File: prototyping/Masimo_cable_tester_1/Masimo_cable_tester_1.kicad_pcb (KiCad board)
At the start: 2 copper layers, 70 x 80 mm, 28 parts, among them J1 Touchscreen HMI, J10 MCU Board Power, J16 Debug Connections, J17 Banana Jack, J2 Curiosity Nano AVR128DB48, J3 Conn_01x28_Socket, J4 Barrel Jack 9V, J5 MicroSD PinHeader, J6 SFML-110-02-L-D-A, J7 HMI Power Toggle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

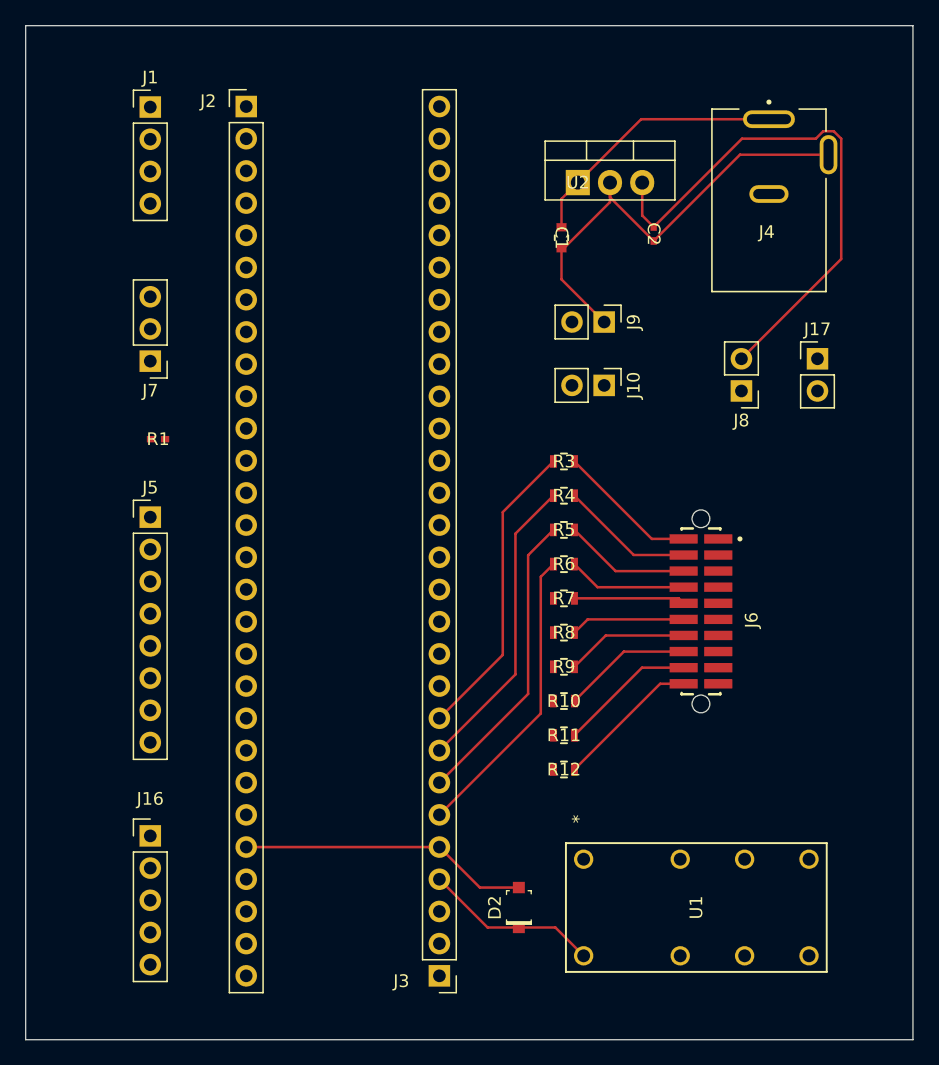
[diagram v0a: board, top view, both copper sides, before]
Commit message: Prototype Schematic and PCB Update
Updated the prototype schematic and PCB. Put all analog if tags on 1 side for easier PCB tracing. By doing this I also changed the location of the Rsig, CD, and CS locations on the MC.
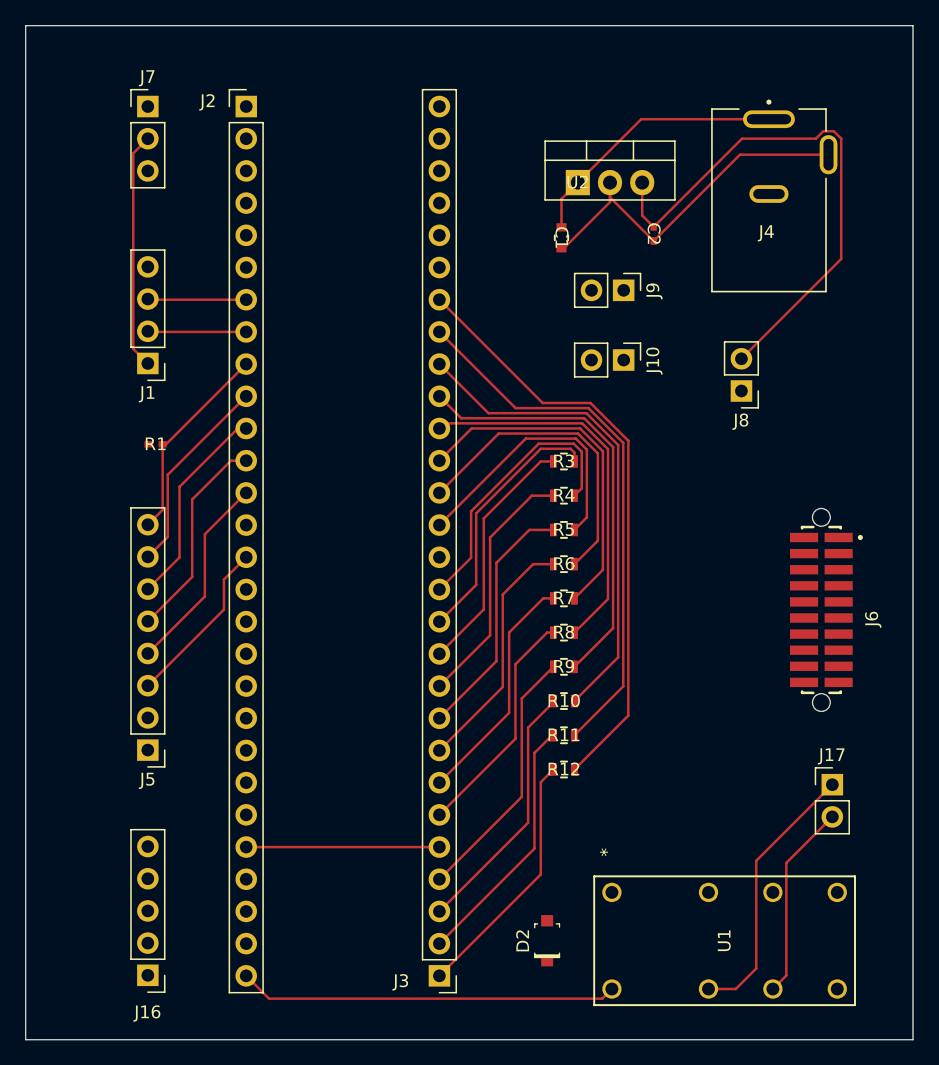
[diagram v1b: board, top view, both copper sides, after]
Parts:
- moved J17 33.6 mm to (144.0, 111.5)
- moved J1 20.2 mm to (90.0, 78.3), turned to 180 degrees
- moved J7 20.1 mm to (90.0, 58.0), turned to 0 degrees
- moved J5 18.4 mm to (90.0, 108.8), turned to 180 degrees
- moved J16 11.0 mm to (90.0, 126.5), turned to 180 degrees
- moved J6 9.50 mm to (143.1, 97.7)
- moved D2 3.44 mm to (121.5, 123.8)
- moved U1 3.44 mm to (126.6, 127.6)
- moved J9 2.94 mm to (127.5, 72.5)
- moved J10 2.52 mm to (127.5, 78.0)
- moved R1 0.45 mm to (90.6, 84.6)
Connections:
- J17 pad 2: BJ1 -> BJ2
- J2 pad 10: unconnected-(J2-Pin_10-Pad10) -> CS
- J2 pad 18: CTRL 10 -> unconnected-(J2-Pin_18-Pad18)
- J2 pad 19: CTRL 9 -> unconnected-(J2-Pin_19-Pad19)
- J2 pad 20: CTRL 8 -> unconnected-(J2-Pin_20-Pad20)
- J2 pad 21: CTRL 7 -> unconnected-(J2-Pin_21-Pad21)
- J2 pad 22: CTRL 6 -> unconnected-(J2-Pin_22-Pad22)
- J2 pad 23: CTRL 5 -> unconnected-(J2-Pin_23-Pad23)
- J2 pad 28: unconnected-(J2-Pin_28-Pad28) -> RSig
- J2 pad 9: unconnected-(J2-Pin_9-Pad9) -> CD
- J3 pad 1: unconnected-(J3-Pin_1-Pad1) -> CTRL 10
- J3 pad 10: ADC 10 -> CTRL 2
- J3 pad 11: ADC 9 -> CTRL 1
- J3 pad 12: CS -> ADC 1
- J3 pad 13: CD -> ADC 2
- J3 pad 15: ADC 8 -> ADC 3
- J3 pad 16: ADC 7 -> ADC 4
- J3 pad 17: ADC 6 -> ADC 5
- J3 pad 18: ADC 5 -> ADC 6
- J3 pad 19: ADC 4 -> ADC 7
- J3 pad 2: unconnected-(J3-Pin_2-Pad2) -> CTRL 9
- J3 pad 20: ADC 3 -> ADC 8
- J3 pad 21: ADC 2 -> ADC 9
- J3 pad 22: ADC 1 -> ADC 10
- J3 pad 3: unconnected-(J3-Pin_3-Pad3) -> CTRL 8
- J3 pad 4: RSig -> CTRL 7
- J3 pad 6: CTRL 4 -> CTRL 6
- J3 pad 7: CTRL 3 -> CTRL 5
- J3 pad 8: CTRL 2 -> CTRL 4
- J3 pad 9: CTRL 1 -> CTRL 3
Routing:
- net ADC 10: track 11.4 -> 47.2 mm
- net ADC 9: track 10.8 -> 42.8 mm
- net ADC 8: track 10.2 -> 38.4 mm
- net ADC 7: track 9.64 -> 34.0 mm
- net BJ1: track 0.00 -> 21.4 mm
- net ADC 6: track 9.05 -> 29.9 mm
- net CTRL 7: track 0.00 -> 20.5 mm
- net CTRL 8: track 0.00 -> 20.3 mm
- net CTRL 9: track 0.00 -> 20.2 mm
- net CTRL 10: track 0.00 -> 20.0 mm
- net CTRL 5: track 0.00 -> 18.7 mm
- net Net-(J1-Pin_1): track 0.00 -> 18.7 mm
- net ADC 5: track 8.78 -> 27.2 mm
- net CTRL 6: track 0.00 -> 18.4 mm
- net DO: track 0.00 -> 16.6 mm
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
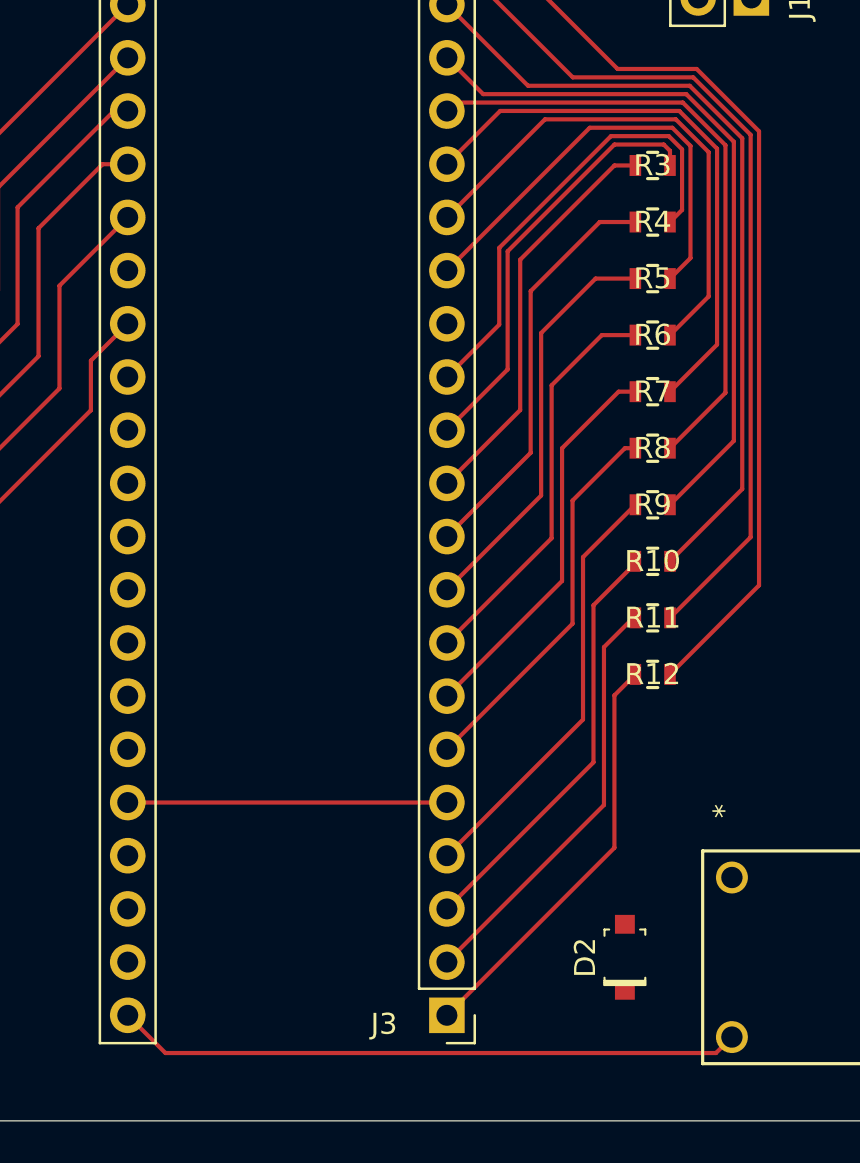
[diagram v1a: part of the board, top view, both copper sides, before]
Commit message: Prototype PCB Changes
A few routing changes to the Prototype PCB.
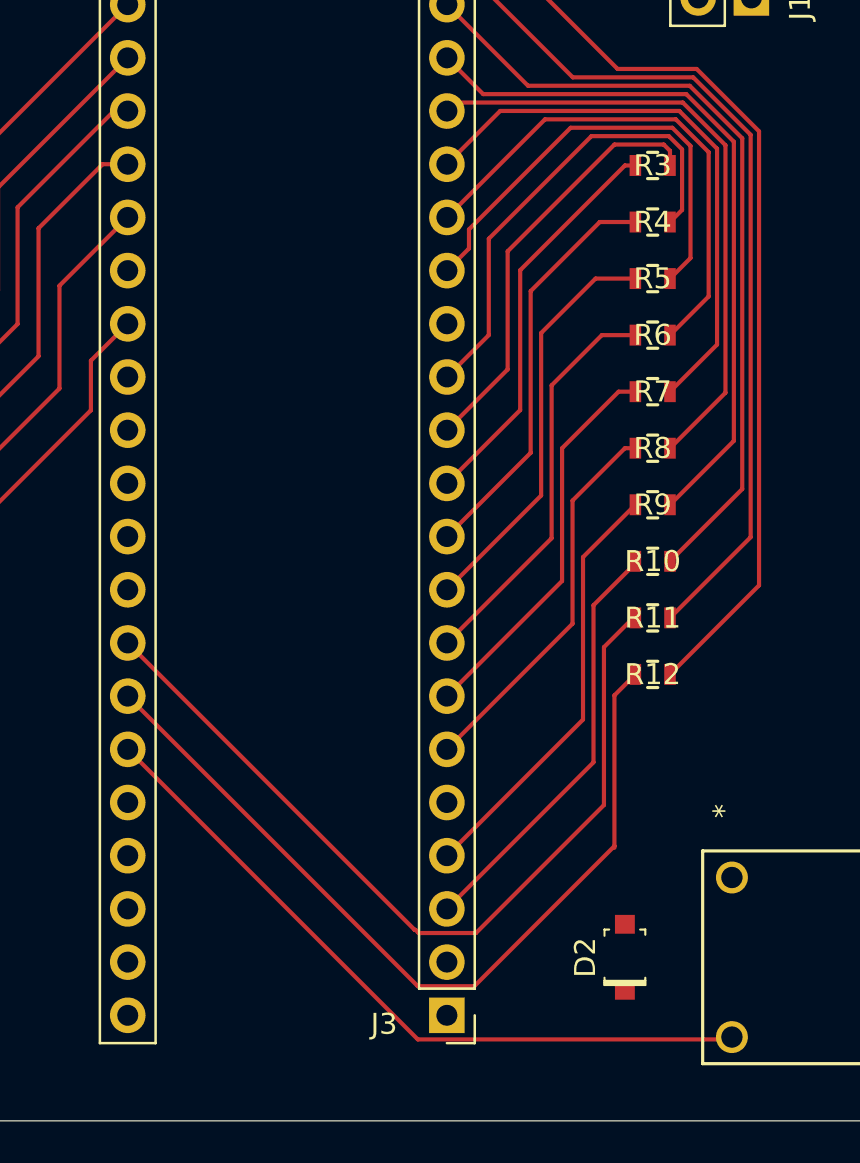
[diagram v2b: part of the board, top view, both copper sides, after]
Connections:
- J2 pad 21: unconnected-(J2-Pin_21-Pad21) -> CTRL 9
- J2 pad 22: unconnected-(J2-Pin_22-Pad22) -> CTRL 10
- J2 pad 23: unconnected-(J2-Pin_23-Pad23) -> RSig
- J2 pad 28: RSig -> unconnected-(J2-Pin_28-Pad28)
- J3 pad 1: CTRL 10 -> unconnected-(J3-Pin_1-Pad1)
- J3 pad 2: CTRL 9 -> unconnected-(J3-Pin_2-Pad2)
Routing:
- net CTRL 10: track 20.0 -> 40.4 mm
- net CTRL 9: track 20.2 -> 40.6 mm
- net GND: track 58.1 -> 42.9 mm
- net RSig: track 29.9 -> 34.6 mm
- net ADC 2: track 22.1 -> 22.7 mm
- net ADC 3: track 21.6 -> 22.1 mm
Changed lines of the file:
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@@
 	(net 7 "Rx1")
 	(net 8 "unconnected-(J2-Pin_17-Pad17)")
-	(net 9 "unconnected-(J2-Pin_23-Pad23)")
-	(net 10 "unconnected-(J2-Pin_22-Pad22)")
+	(net 9 "unconnected-(J2-Pin_28-Pad28)")
+	(net 10 "unconnected-(J3-Pin_1-Pad1)")
 	(net 11 "CTRL 5")
 	(net 12 "unconnected-(J2-Pin_6-Pad6)")
@@
 	(net 49 "ADC 4")
 	(net 50 "Net-(J10-Pin_1)")
-	(net 51 "unconnected-(J2-Pin_21-Pad21)")
+	(net 51 "unconnected-(J3-Pin_2-Pad2)")
 	(net 52 "ADC 6")
 	(net 53 "VBUS 5V")
@@
 			)
 			(remove_unused_layers no)
-			(net 51 "unconnected-(J2-Pin_21-Pad21)")
+			(net 17 "CTRL 9")
 			(pinfunction "Pin_21")
 			(pintype "passive")
@@
 			)
 			(remove_unused_layers no)
-			(net 10 "unconnected-(J2-Pin_22-Pad22)")
+			(net 25 "CTRL 10")
 			(pinfunction "Pin_22")
 			(pintype "passive")
@@
 			)
 			(remove_unused_layers no)
-			(net 9 "unconnected-(J2-Pin_23-Pad23)")
+			(net 4 "RSig")
 			(pinfunction "Pin_23")
 			(pintype "passive")
@@
 			)
 			(remove_unused_layers no)
-			(net 4 "RSig")
+			(net 9 "unconnected-(J2-Pin_28-Pad28)")
 			(pinfunction "Pin_28")
 			(pintype "passive")
@@
 			)
 			(remove_unused_layers no)
-			(net 25 "CTRL 10")
+			(net 10 "unconnected-(J3-Pin_1-Pad1)")
 			(pinfunction "Pin_1")
 			(pintype "passive")
@@
 			)
 			(remove_unused_layers no)
-			(net 17 "CTRL 9")
+			(net 51 "unconnected-(J3-Pin_2-Pad2)")
 			(pinfunction "Pin_2")
 			(pintype "passive")
@@
 	)
 	(segment
-		(start 97.76 116.42)
-		(end 113 116.42)
-		(width 0.2)
-		(layer "F.Cu")
-		(net 1)
-	)
-	(segment
 		(start 126.46 65.1606)
 		(end 126.46 64)
@@
 	)
 	(segment
-		(start 125.848001 128.381999)
-		(end 126.61 127.62)
+		(start 111.611 127.731)
+		(end 126.499 127.731)
 		(width 0.2)
 		(layer "F.Cu")
@@
 	)
 	(segment
-		(start 99.561999 128.381999)
-		(end 125.848001 128.381999)
+		(start 126.499 127.731)
+		(end 126.61 127.62)
 		(width 0.2)
 		(layer "F.Cu")
@@
 	)
 	(segment
-		(start 97.76 126.58)
-		(end 99.561999 128.381999)
+		(start 97.76 113.88)
+		(end 111.611 127.731)
 		(width 0.2)
 		(layer "F.Cu")
@@
 	)
 	(segment
-		(start 121.898224 107.601776)
-		(end 122 107.601776)
+		(start 111.5 122.5)
+		(end 111.651 122.651)
 		(width 0.2)
 		(layer "F.Cu")
@@
 	)
 	(segment
-		(start 113 124.04)
+		(start 114.389 122.651)
 		(end 120.5 116.54)
 		(width 0.2)
@@
 	)
 	(segment
+		(start 111.46 122.5)
+		(end 111.5 122.5)
+		(width 0.2)
+		(layer "F.Cu")
+		(net 17)
+	)
+	(segment
+		(start 97.76 108.8)
+		(end 111.46 122.5)
+		(width 0.2)
+		(layer "F.Cu")
+		(net 17)
+	)
+	(segment
+		(start 121.898224 107.601776)
+		(end 122 107.601776)
+		(width 0.2)
+		(layer "F.Cu")
+		(net 17)
+	)
+	(segment
 		(start 120.5 109)
 		(end 121.898224 107.601776)
@@
 	)
 	(segment
+		(start 111.651 122.651)
+		(end 114.389 122.651)
+		(width 0.2)
+		(layer "F.Cu")
+		(net 17)
+	)
+	(segment
 		(start 120.5 116.54)
 		(end 120.5 109)
@@
 	)
 	(segment
-		(start 113 126.58)
-		(end 121 118.58)
+		(start 121 118.5)
+		(end 121 111.302)
 		(width 0.2)
 		(layer "F.Cu")
@@
 	)
 	(segment
-		(start 121 118.58)
-		(end 121 111.302)
+		(start 114.309 125.191)
+		(end 121 118.5)
 		(width 0.2)
 		(layer "F.Cu")
@@
 	)
 	(segment
+		(start 97.76 111.34)
+		(end 111.611 125.191)
+		(width 0.2)
+		(layer "F.Cu")
+		(net 25)
+	)
+	(segment
+		(start 121 118.58)
+		(end 121 118.5)
+		(width 0.2)
+		(layer "F.Cu")
+		(net 25)
+	)
+	(segment
+		(start 111.611 125.191)
+		(end 114.309 125.191)
+		(width 0.2)
+		(layer "F.Cu")
+		(net 25)
+	)
+	(segment
 		(start 119.5 112.46)
 		(end 119.5 104.701332)
@@
 	)
 	(segment
-		(start 113 91.02)
-		(end 119.822 84.198)
+		(start 124.6318 90.421844)
+		(end 124.6318 85.0647)
 		(width 0.2)
 		(layer "F.Cu")
@@
 	)
 	(segment
-		(start 123.7651 84.198)
-		(end 124.6318 85.0647)
+		(start 114.05388 89.05388)
+		(end 114.05388 89.96612)
 		(width 0.2)
 		(layer "F.Cu")
@@
 	)
 	(segment
-		(start 124.6318 90.421844)
-		(end 123.6532 91.400444)
+		(start 124.6318 85.0647)
+		(end 123.7651 84.198)
 		(width 0.2)
 		(layer "F.Cu")
@@
 	)
 	(segment
-		(start 119.822 84.198)
-		(end 123.7651 84.198)
+		(start 123.6532 91.400444)
+		(end 124.6318 90.421844)
 		(width 0.2)
 		(layer "F.Cu")
@@
 	)
 	(segment
-		(start 124.6318 85.0647)
-		(end 124.6318 90.421844)
+		(start 123.7651 84.198)
+		(end 118.90976 84.198)
 		(width 0.2)
 		(layer "F.Cu")
@@
 	)
 	(segment
-		(start 115.5 89.9329)
-		(end 120.8339 84.599)
+		(start 114.05388 89.96612)
+		(end 113 91.02)
+		(width 0.2)
+		(layer "F.Cu")
+		(net 39)
+	)
+	(segment
+		(start 118.90976 84.198)
+		(end 114.05388 89.05388)
+		(width 0.2)
+		(layer "F.Cu")
+		(net 39)
+	)
+	(segment
+		(start 115 94.1)
+		(end 115 89.5)
 		(width 0.2)
 		(layer "F.Cu")
@@
 	)
 	(segment
-		(start 123.599 84.599)
-		(end 124.2308 85.2308)
+		(start 115 89.5)
+		(end 119.901 84.599)
 		(width 0.2)
 		(layer "F.Cu")
@@
 	(segment
 		(start 113 96.1)
-		(end 115.5 93.6)
+		(end 115 94.1)
 		(width 0.2)
 		(layer "F.Cu")
@@
 	)
 	(segment
-		(start 115.5 93.6)
-		(end 115.5 89.9329)
+		(start 119.901 84.599)
+		(end 123.599 84.599)
 		(width 0.2)
 		(layer "F.Cu")
@@
 	)
 	(segment
-		(start 120.8339 84.599)
-		(end 123.599 84.599)
+		(start 123.599 84.599)
+		(end 124.2308 85.2308)
 		(width 0.2)
 		(layer "F.Cu")
@@
 	)
 	(segment
-		(start 116.5 90.5)
-		(end 121 86)
+		(start 116.5 97.68)
+		(end 116.5 91)
 		(width 0.2)
 		(layer "F.Cu")
@@
 	)
 	(segment
-		(start 121 86)
+		(start 121.5 86)
 		(end 122 86)
 		(width 0.2)
@@
 	)
 	(segment
-		(start 116.5 97.68)
-		(end 116.5 90.5)
+		(start 116.5 91)
+		(end 121.5 86)
 		(width 0.2)
 		(layer "F.Cu")
